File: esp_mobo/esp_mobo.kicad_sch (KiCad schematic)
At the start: 59 parts, among them J1 Conn_01x04_Pin, J10 Conn_01x03_Pin, J11 Conn_01x03_Pin, J12 Conn_01x03_Pin, J13 Conn_01x03_Pin, J14 Conn_01x03_Pin, J15 Conn_01x03_Pin, J16 Conn_01x02_Pin, J2 Screw_Terminal_01x02, J3 Conn_01x03_Pin, J4 Conn_01x03_Pin, J5 Conn_01x03_Pin, J6 Conn_01x03_Pin, J7 Conn_01x03_Pin, J8 Conn_01x03_Pin, J9 Conn_01x03_Pin, U1 ESP32-DevKitC, U2 74AHCT125, U3 PC847, U4 PC847, U5 BME280

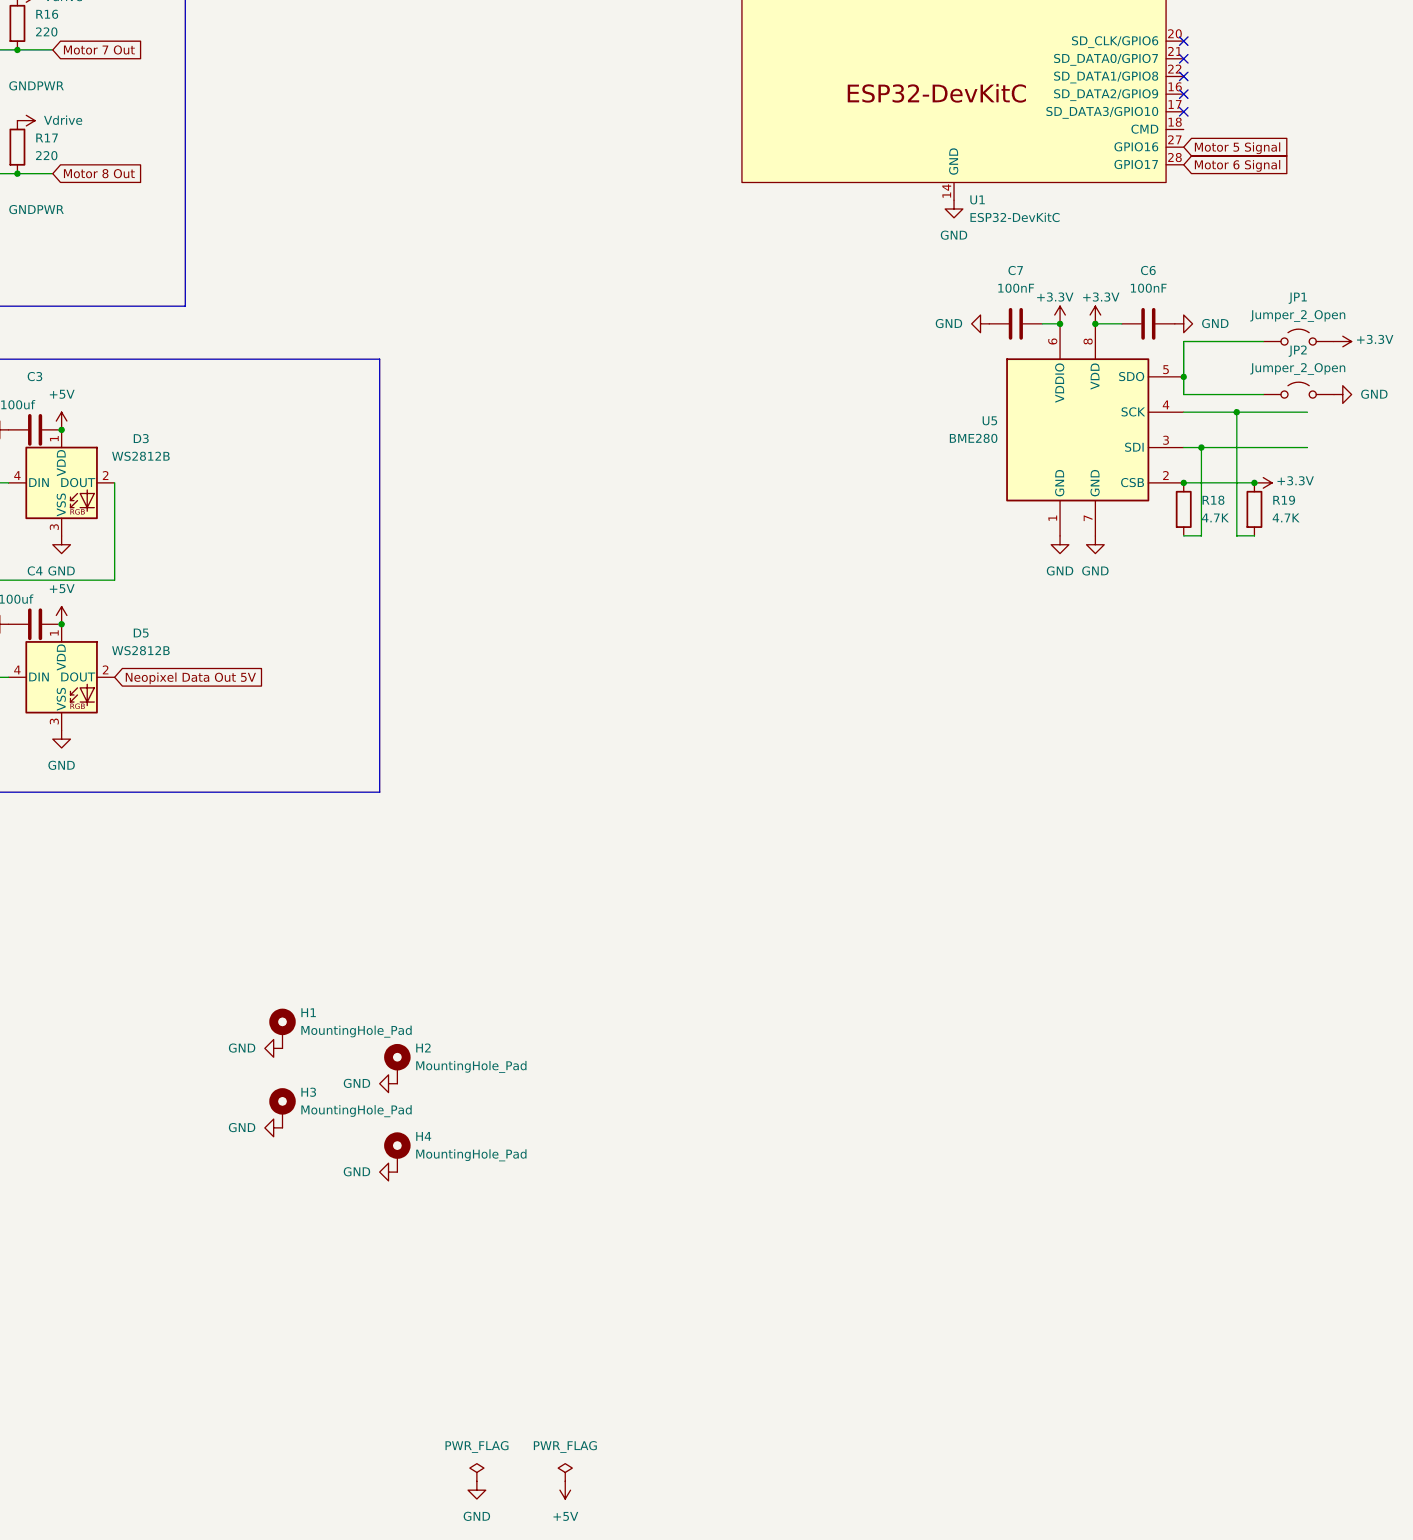
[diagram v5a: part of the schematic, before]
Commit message: Update ESC Mobo with BME280
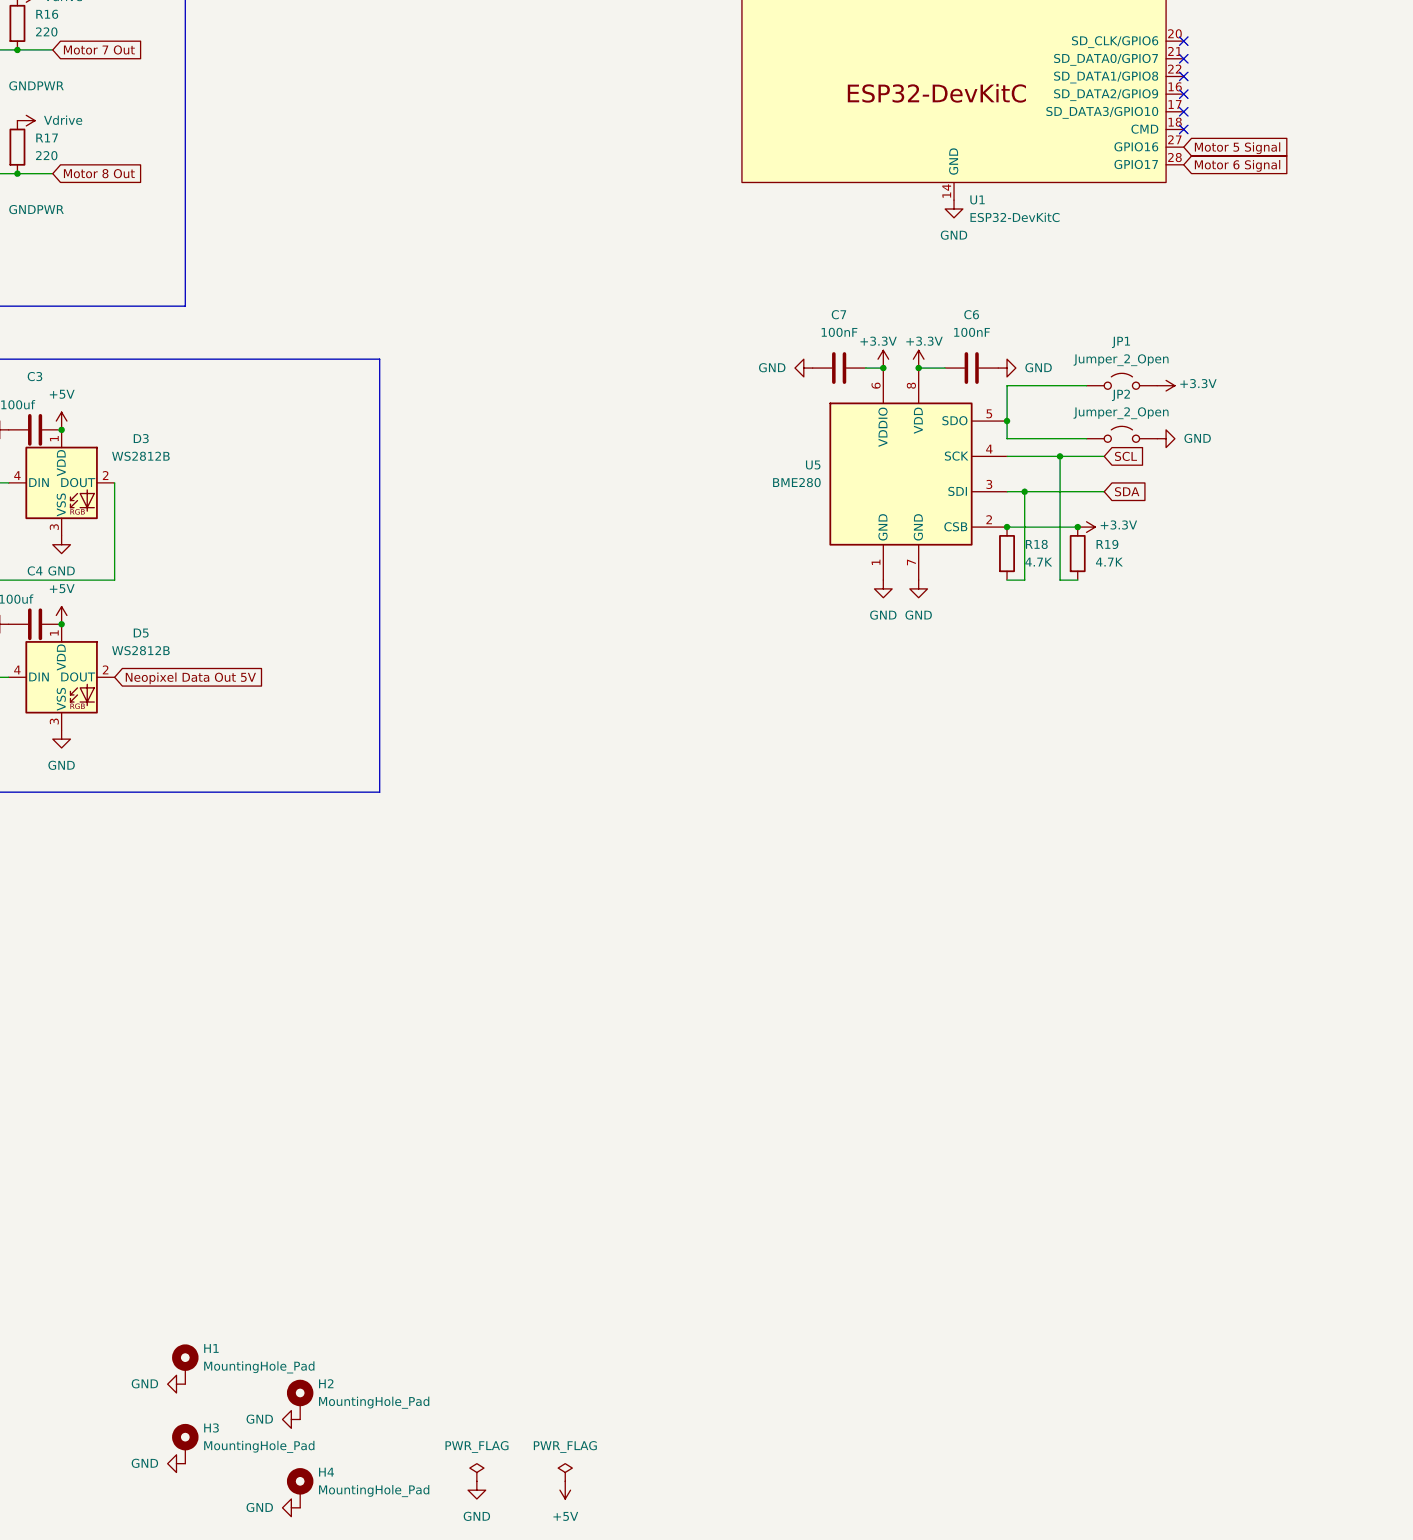
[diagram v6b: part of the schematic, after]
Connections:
- net SCL: now also R19.2, U5.4 (SCK)
- net SDA: now also R18.2, U5.3 (SDI)
- no-connect marks 5 -> 6
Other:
- moved on the sheet: C6, C7, H1, H2, H3, H4, JP1, JP2, R18, R19, U5

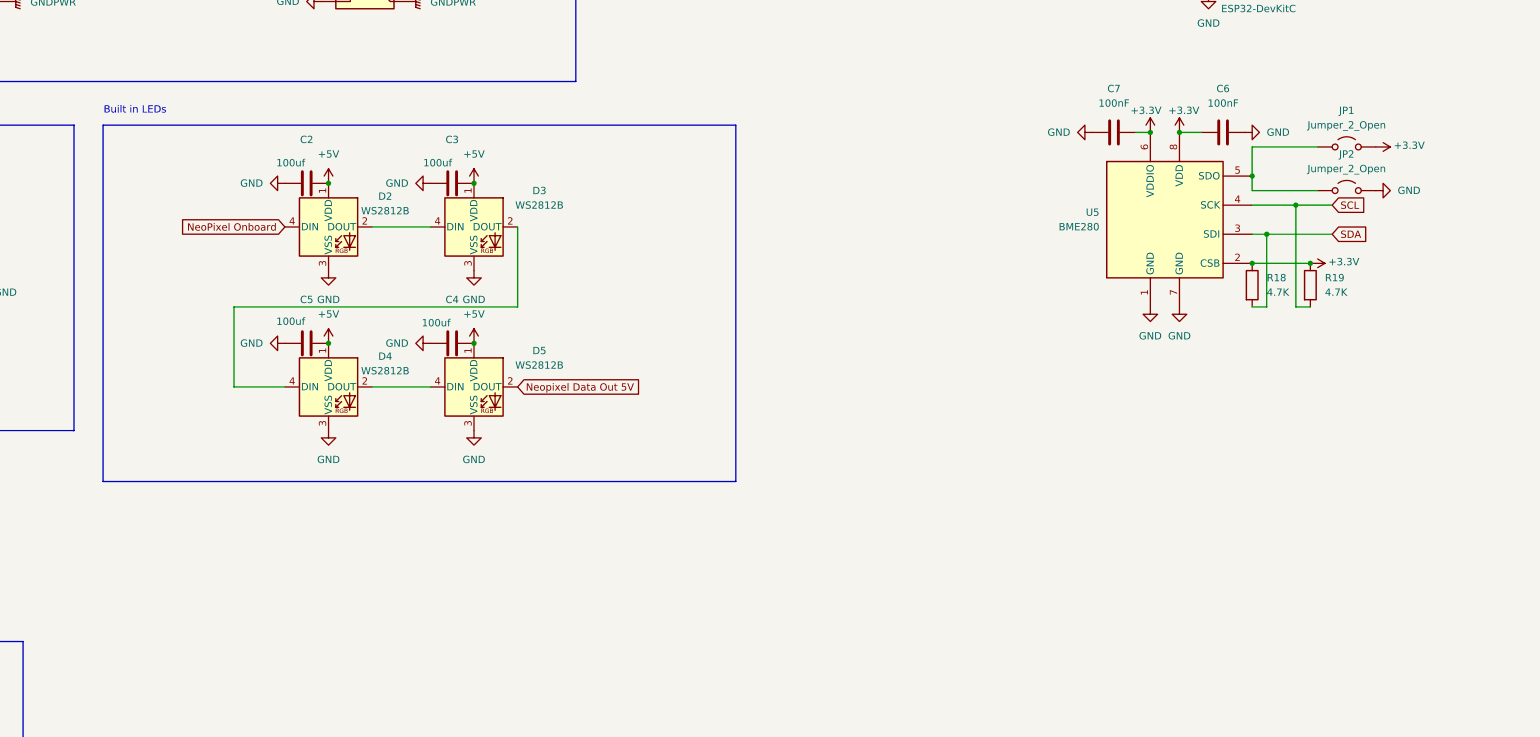
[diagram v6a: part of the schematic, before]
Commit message: Update ESC Mobo with board
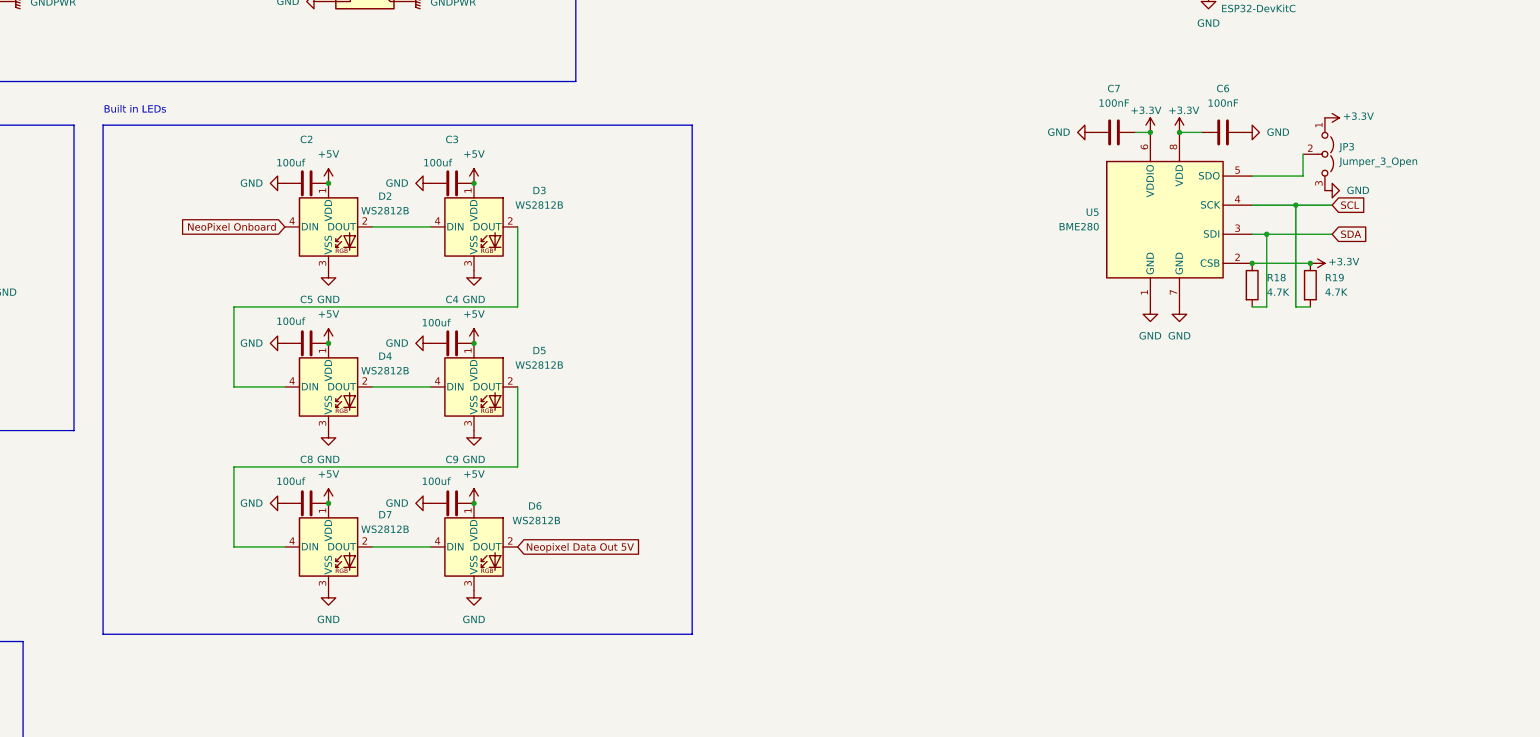
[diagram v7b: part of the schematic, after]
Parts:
- removed JP1: Jumper_2_Open, Connector_PinHeader_2.54mm:PinHeader_1x02_P2.54mm_Vertical, symbol Jumper:Jumper_2_Open
- removed JP2: Jumper_2_Open, symbol Jumper:Jumper_2_Open
- added C8, C9: 100uf, Capacitor_SMD:C_0603_1608Metric, symbol Device:C
- added D6, D7: WS2812B, LED_SMD:LED_WS2812B_PLCC4_5.0x5.0mm_P3.2mm, symbol LED:WS2812B
- added JP3: Jumper_3_Open, Connector_PinHeader_2.54mm:PinHeader_1x03_P2.54mm_Vertical, symbol Jumper:Jumper_3_Open
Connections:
- net +3.3V: now also JP3.1 (A)
- net +5V: now also C8.2, C9.2, D6.1 (VDD), D7.1 (VDD)
- net GND: now also C8.1, C9.1, D6.3 (VSS), D7.3 (VSS), JP3.3 (B)
- net Neopixel Data Out 5V: now also D6.2 (DOUT); no longer D5.2 (DOUT)
- net at U5.5 (SDO): now also JP3.2 (C)
- new net: D5.2 (DOUT), D7.4 (DIN)
- new net: D6.4 (DIN), D7.2 (DOUT)

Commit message: Update ESC Mobo
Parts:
- removed J16: Conn_01x02_Pin, Connector_PinHeader_2.54mm:PinHeader_1x02_P2.54mm_Vertical, symbol Connector:Conn_01x02_Pin
- added JP1: Jumper_2_Open, symbol Jumper:Jumper_2_Open
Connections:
- net +5V: now also J1.4 (Pin_4), JP1.2 (B); no longer J1.1 (Pin_1)
- net GND: now also J1.1 (Pin_1); no longer J1.4 (Pin_4)
- net Vdrive: now also JP1.1 (A)
